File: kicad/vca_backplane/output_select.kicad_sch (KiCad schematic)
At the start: 54 parts, among them J13 AudioJack_729JH, J9 AudioJack_729JH, U10 NE5532, U12 DG442xY, U4 MCP4822, U5 PCA9555PW, U6 DG442xY, U7 AS3360, U9 DG442xY

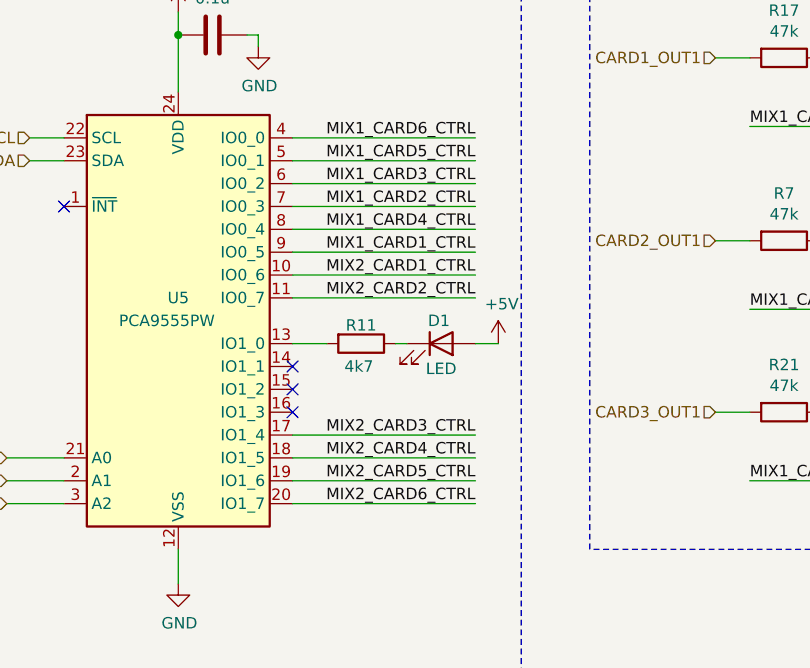
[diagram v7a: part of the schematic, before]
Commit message: remap some pins
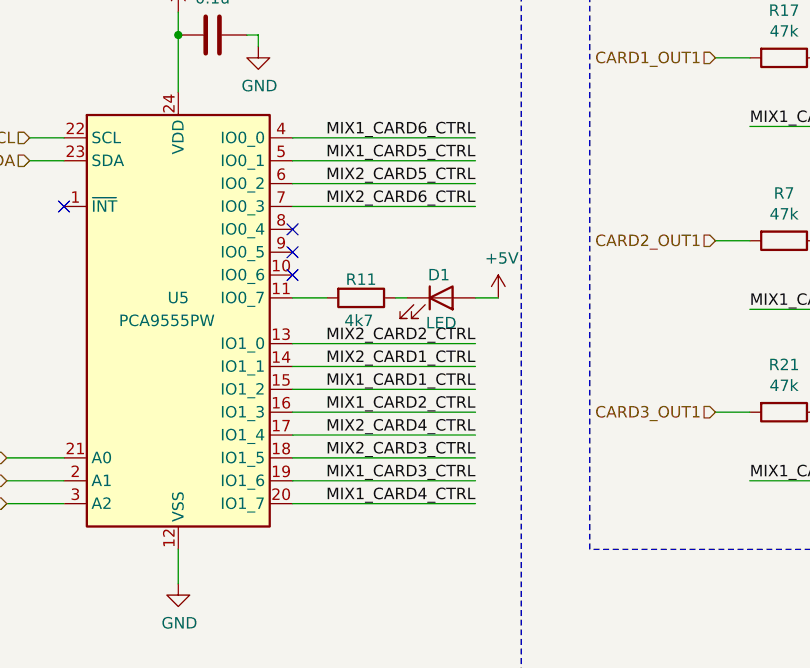
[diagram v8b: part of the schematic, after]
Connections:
- net MIX1_CARD1_CTRL: now also U5.15 (IO1_2); no longer U5.9 (IO0_5)
- net MIX1_CARD2_CTRL: now also U5.16 (IO1_3); no longer U5.7 (IO0_3)
- net MIX1_CARD3_CTRL: now also U5.19 (IO1_6); no longer U5.6 (IO0_2)
- net MIX1_CARD4_CTRL: now also U5.20 (IO1_7); no longer U5.8 (IO0_4)
- net MIX2_CARD1_CTRL: now also U5.14 (IO1_1); no longer U5.10 (IO0_6)
- net MIX2_CARD2_CTRL: now also U5.13 (IO1_0); no longer U5.11 (IO0_7)
- net MIX2_CARD3_CTRL: now also U5.18 (IO1_5); no longer U5.17 (IO1_4)
- net MIX2_CARD4_CTRL: now also U5.17 (IO1_4); no longer U5.18 (IO1_5)
- net MIX2_CARD5_CTRL: now also U5.6 (IO0_2); no longer U5.19 (IO1_6)
- net MIX2_CARD6_CTRL: now also U5.7 (IO0_3); no longer U5.20 (IO1_7)
- net at R11.2: now also U5.11 (IO0_7); no longer U5.13 (IO1_0)
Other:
- moved on the sheet: D1, R11
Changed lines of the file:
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@@
   )
   (no_connect (at 334.01 181.61))
-  (no_connect (at 62.23 72.39))
-  (no_connect (at 62.23 69.85))
-  (no_connect (at 62.23 67.31))
+  (no_connect (at 62.23 57.15))
   (no_connect (at 36.83 49.53))
+  (no_connect (at 62.23 54.61))
   (no_connect (at 334.01 142.24))
+  (no_connect (at 62.23 52.07))
   (wire (pts (xy 283.21 181.61) (xy 289.56 181.61))
     (stroke (width 0) (type default))
@@
     (stroke (width 0) (type default))
   )
-  (wire (pts (xy 62.23 52.07) (xy 82.55 52.07))
+  (wire (pts (xy 62.23 64.77) (xy 82.55 64.77))
     (stroke (width 0) (type default))
   )
@@
     (stroke (width 0) (type dash))
   )
-  (wire (pts (xy 62.23 59.69) (xy 82.55 59.69))
+  (wire (pts (xy 62.23 72.39) (xy 82.55 72.39))
     (stroke (width 0) (type default))
   )
@@
     (stroke (width 0) (type default))
   )
-  (wire (pts (xy 62.23 54.61) (xy 82.55 54.61))
+  (wire (pts (xy 62.23 67.31) (xy 82.55 67.31))
     (stroke (width 0) (type default))
   )
@@
     (stroke (width 0) (type default))
   )
-  (wire (pts (xy 62.23 64.77) (xy 66.04 64.77))
+  (wire (pts (xy 62.23 59.69) (xy 66.04 59.69))
     (stroke (width 0) (type default))
   )
@@
     (stroke (width 0) (type default))
   )
-  (wire (pts (xy 73.66 64.77) (xy 74.93 64.77))
+  (wire (pts (xy 73.66 59.69) (xy 74.93 59.69))
     (stroke (width 0) (type default))
   )
@@
     (stroke (width 0) (type default))
   )
-  (wire (pts (xy 85.09 64.77) (xy 82.55 64.77))
+  (wire (pts (xy 85.09 59.69) (xy 82.55 59.69))
     (stroke (width 0) (type default))
   )
@@
     (stroke (width 0) (type default))
   )
-  (wire (pts (xy 62.23 57.15) (xy 82.55 57.15))
+  (wire (pts (xy 62.23 69.85) (xy 82.55 69.85))
     (stroke (width 0) (type default))
   )
@@
     (effects (font (size 1.27 1.27)) (justify left bottom))
   )
-  (label "MIX1_CARD1_CTRL" (at 82.55 54.61 180) (fields_autoplaced)
+  (label "MIX1_CARD1_CTRL" (at 82.55 69.85 180) (fields_autoplaced)
     (effects (font (size 1.27 1.27)) (justify right bottom))
   )
@@
     (effects (font (size 1.27 1.27)) (justify right bottom))
   )
-  (label "MIX1_CARD4_CTRL" (at 82.55 52.07 180) (fields_autoplaced)
-    (effects (font (size 1.27 1.27)) (justify right bottom))
-  )
-  (label "MIX1_CARD3_CTRL" (at 82.55 46.99 180) (fields_autoplaced)
+  (label "MIX1_CARD4_CTRL" (at 82.55 82.55 180) (fields_autoplaced)
+    (effects (font (size 1.27 1.27)) (justify right bottom))
+  )
+  (label "MIX1_CARD3_CTRL" (at 82.55 80.01 180) (fields_autoplaced)
     (effects (font (size 1.27 1.27)) (justify right bottom))
   )
@@
     (effects (font (size 1.27 1.27)) (justify right bottom))
   )
-  (label "MIX2_CARD3_CTRL" (at 82.55 74.93 180) (fields_autoplaced)
+  (label "MIX2_CARD3_CTRL" (at 82.55 77.47 180) (fields_autoplaced)
     (effects (font (size 1.27 1.27)) (justify right bottom))
   )
@@
     (effects (font (size 1.27 1.27)) (justify left bottom))
   )
-  (label "MIX2_CARD4_CTRL" (at 82.55 77.47 180) (fields_autoplaced)
+  (label "MIX2_CARD4_CTRL" (at 82.55 74.93 180) (fields_autoplaced)
     (effects (font (size 1.27 1.27)) (justify right bottom))
   )
@@
     (effects (font (size 1.27 1.27)) (justify left bottom))
   )
-  (label "MIX2_CARD1_CTRL" (at 82.55 57.15 180) (fields_autoplaced)
-    (effects (font (size 1.27 1.27)) (justify right bottom))
-  )
-  (label "MIX2_CARD5_CTRL" (at 82.55 80.01 180) (fields_autoplaced)
-    (effects (font (size 1.27 1.27)) (justify right bottom))
-  )
-  (label "MIX2_CARD2_CTRL" (at 82.55 59.69 180) (fields_autoplaced)
+  (label "MIX2_CARD1_CTRL" (at 82.55 67.31 180) (fields_autoplaced)
+    (effects (font (size 1.27 1.27)) (justify right bottom))
+  )
+  (label "MIX2_CARD5_CTRL" (at 82.55 46.99 180) (fields_autoplaced)
+    (effects (font (size 1.27 1.27)) (justify right bottom))
+  )
+  (label "MIX2_CARD2_CTRL" (at 82.55 64.77 180) (fields_autoplaced)
     (effects (font (size 1.27 1.27)) (justify right bottom))
   )
@@
     (effects (font (size 1.27 1.27)) (justify right bottom))
   )
-  (label "MIX2_CARD6_CTRL" (at 82.55 82.55 180) (fields_autoplaced)
-    (effects (font (size 1.27 1.27)) (justify right bottom))
-  )
-  (label "MIX1_CARD2_CTRL" (at 82.55 49.53 180) (fields_autoplaced)
+  (label "MIX2_CARD6_CTRL" (at 82.55 49.53 180) (fields_autoplaced)
+    (effects (font (size 1.27 1.27)) (justify right bottom))
+  )
+  (label "MIX1_CARD2_CTRL" (at 82.55 72.39 180) (fields_autoplaced)
     (effects (font (size 1.27 1.27)) (justify right bottom))
   )
@@
     )
   )
-  (symbol (lib_id "Device:LED") (at 78.74 64.77 0) (unit 1)
-    (in_bom yes) (on_board yes) (dnp no)
-    (property "Reference" "D1" (at 78.486 62.23 0)
-      (effects (font (size 1.27 1.27)))
-    )
-    (property "Value" "LED" (at 78.74 67.564 0)
-      (effects (font (size 1.27 1.27)))
-    )
-    (property "Footprint" "LED_SMD:LED_0603_1608Metric" (at 78.74 64.77 0)
-      (effects (font (size 1.27 1.27)) hide)
-    )
-    (property "Datasheet" "~" (at 78.74 64.77 0)
-      (effects (font (size 1.27 1.27)) hide)
-    )
-    (property "LCSC" "C2286" (at 78.74 64.77 0)
+  (symbol (lib_id "Device:LED") (at 78.74 59.69 0) (unit 1)
+    (in_bom yes) (on_board yes) (dnp no)
+    (property "Reference" "D1" (at 78.486 57.15 0)
+      (effects (font (size 1.27 1.27)))
+    )
+    (property "Value" "LED" (at 78.74 62.484 0)
+      (effects (font (size 1.27 1.27)))
+    )
+    (property "Footprint" "LED_SMD:LED_0603_1608Metric" (at 78.74 59.69 0)
+      (effects (font (size 1.27 1.27)) hide)
+    )
+    (property "Datasheet" "~" (at 78.74 59.69 0)
+      (effects (font (size 1.27 1.27)) hide)
+    )
+    (property "LCSC" "C2286" (at 78.74 59.69 0)
       (effects (font (size 1.27 1.27)) hide)
     )
@@
     )
   )
-  (symbol (lib_id "Device:R") (at 69.85 64.77 270) (unit 1)
-    (in_bom yes) (on_board yes) (dnp no)
-    (property "Reference" "R11" (at 69.85 62.738 90)
-      (effects (font (size 1.27 1.27)))
-    )
-    (property "Value" "4k7" (at 69.596 67.31 90)
-      (effects (font (size 1.27 1.27)))
-    )
-    (property "Footprint" "Resistor_SMD:R_0603_1608Metric" (at 69.85 62.992 90)
-      (effects (font (size 1.27 1.27)) hide)
-    )
-    (property "Datasheet" "~" (at 69.85 64.77 0)
-      (effects (font (size 1.27 1.27)) hide)
-    )
-    (property "LCSC" "C23162" (at 69.85 64.77 0)
+  (symbol (lib_id "Device:R") (at 69.85 59.69 270) (unit 1)
+    (in_bom yes) (on_board yes) (dnp no)
+    (property "Reference" "R11" (at 69.85 57.658 90)
+      (effects (font (size 1.27 1.27)))
+    )
+    (property "Value" "4k7" (at 69.596 62.23 90)
+      (effects (font (size 1.27 1.27)))
+    )
+    (property "Footprint" "Resistor_SMD:R_0603_1608Metric" (at 69.85 57.912 90)
+      (effects (font (size 1.27 1.27)) hide)
+    )
+    (property "Datasheet" "~" (at 69.85 59.69 0)
+      (effects (font (size 1.27 1.27)) hide)
+    )
+    (property "LCSC" "C23162" (at 69.85 59.69 0)
       (effects (font (size 1.27 1.27)) hide)
     )
@@
     )
   )
-  (symbol (lib_id "power:+5V") (at 85.09 64.77 0) (unit 1)
-    (in_bom yes) (on_board yes) (dnp no)
-    (property "Reference" "#PWR0172" (at 85.09 68.58 0)
-      (effects (font (size 1.27 1.27)) hide)
-    )
-    (property "Value" "+5V" (at 85.471 60.3758 0)
-      (effects (font (size 1.27 1.27)))
-    )
-    (property "Footprint" "" (at 85.09 64.77 0)
-      (effects (font (size 1.27 1.27)) hide)
-    )
-    (property "Datasheet" "" (at 85.09 64.77 0)
-      (effects (font (size 1.27 1.27)) hide)
-    )
+  (symbol (lib_id "power:+5V") (at 85.09 59.69 0) (unit 1)
+    (in_bom yes) (on_board yes) (dnp no)
+    (property "Reference" "#PWR0172" (at 85.09 63.5 0)
+      (effects (font (size 1.27 1.27)) hide)
+    )
+    (property "Value" "+5V" (at 85.471 55.2958 0)
+      (effects (font (size 1.27 1.27)))
+    )
+    (property "Footprint" "" (at 85.09 59.69 0)
+      (effects (font (size 1.27 1.27)) hide)
+    )
+    (property "Datasheet" "" (at 85.09 59.69 0)
+      (effects (font (size 1.27 1.27)) hide)
+    )
